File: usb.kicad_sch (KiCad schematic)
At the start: 8 parts, among them J2 USB_C_Receptacle_USB2.0_16P, U3 82400102

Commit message: layout v1
no silkscreen done yet
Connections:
- net USB_DN: now also U3.3, U3.4; no longer U3.1, U3.6
- net USB_DP: now also U3.1, U3.6; no longer U3.3, U3.4
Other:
- moved on the sheet: U3
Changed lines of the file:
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@@
 	(symbol
 		(lib_id "Power_Protection:WE-TVS-82400102")
-		(at 66.04 71.12 90)
+		(at 66.04 71.12 270)
+		(mirror x)
 		(unit 1)
 		(exclude_from_sim no)
@@
 		(dnp no)
 		(property "Reference" "U3"
-			(at 75.438 62.484 90)
+			(at 56.642 62.484 90)
 			(effects
 				(font
@@
 		)
 		(property "Value" "82400102"
-			(at 75.438 65.024 90)
+			(at 56.642 65.024 90)
 			(effects
 				(font
@@
 		)
 		(property "Footprint" "Package_TO_SOT_SMD:SOT-23-6"
-			(at 71.12 71.12 0)
+			(at 60.96 71.12 0)
 			(effects
 				(font
@@
 		)
 		(property "Datasheet" "https://www.we-online.com/components/products/datasheet/82400102.pdf"
-			(at 72.39 71.12 0)
+			(at 59.69 71.12 0)
 			(effects
 				(font

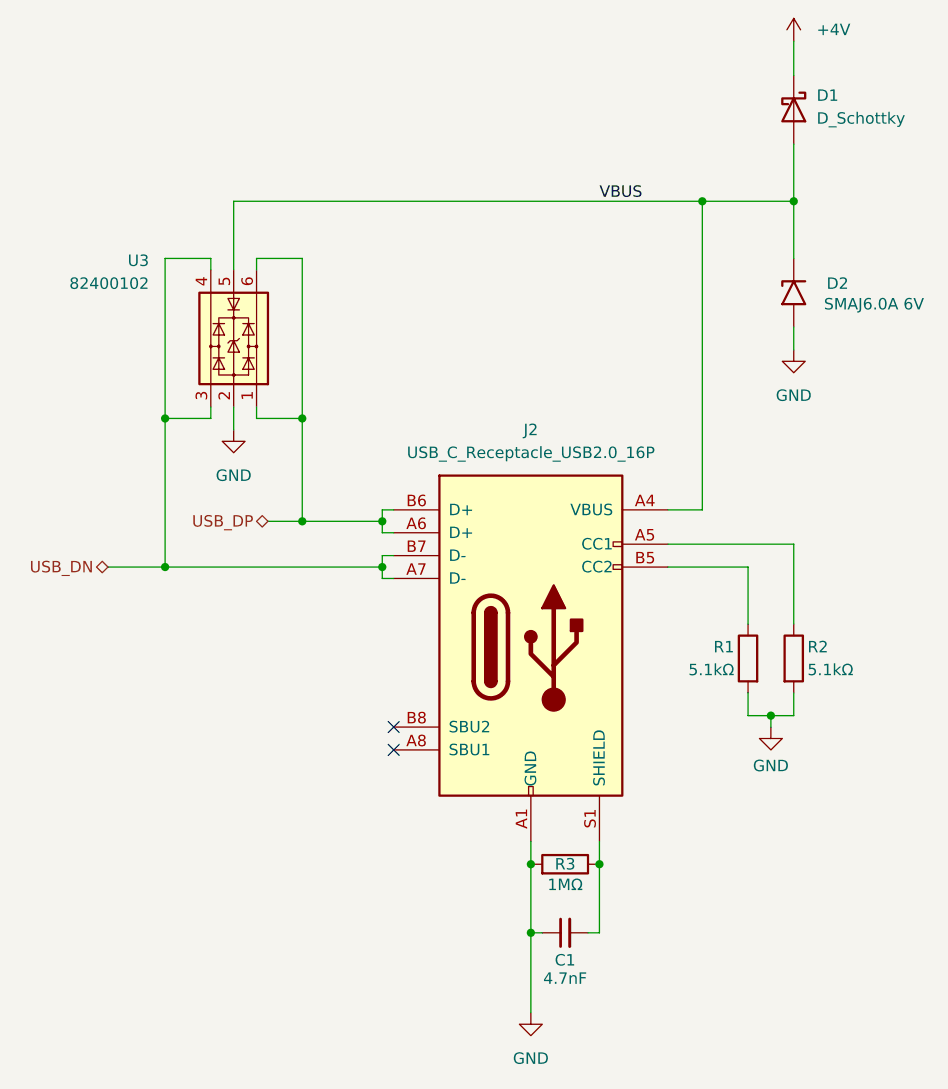
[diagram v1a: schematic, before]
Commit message: Changed PowerSupply idea: use jumper to select PoE or VBUS
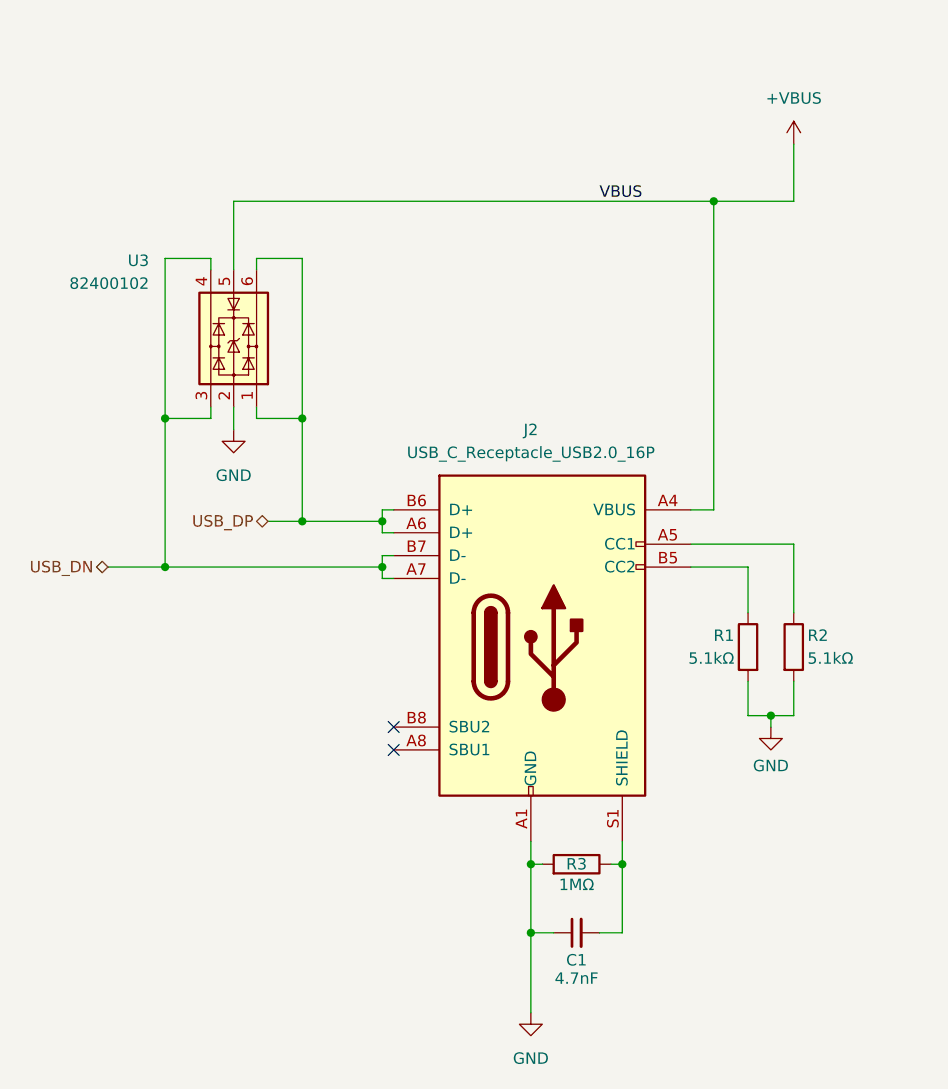
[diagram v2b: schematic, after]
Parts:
- removed D1: D_Schottky, Diode_SMD:D_SMA, symbol Device:D_Schottky
- removed D2: SMAJ6.0A 6V, Diode_SMD:D_SMA, symbol Diode:SMAJ6.0A
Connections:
- net VBUS renamed +VBUS
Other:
- moved on the sheet: C1, J2, R1, R2, R3
